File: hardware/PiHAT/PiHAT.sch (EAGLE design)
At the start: 1 part

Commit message: Bulk copy/paste schematic
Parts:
- added C1, C16, C17, C6, C9: 1uF, SparkFun-Capacitors:CAP0805
- added C10, C11: 0.1uF, SparkFun-Capacitors:CAP0805
- added C12, C13, C14, C15, C3, C4, C5, C7: 0.1uF, SparkFun-Passives:CAP0805
- added C2: 100pF, SparkFun-Capacitors:CAP0805
- added C8: 4.7uF, SparkFun-Capacitors:CAP0805
- added IAQ-CORE: IAQ-CORE, IAQ-CORE:IAQ-CORE
- added J2: (no value), SparkFun-Connectors:M05X2PTH
- added J3: USB-MICROB, SparkFun-Connectors:USB-MICROB
- added LED2, RX, TX: (no value), adafruit:LEDCHIPLED_0805
- added MICS4514: SPARKFUN-SENSORS_MICS-4514, MICS-4514_CO_and_NOx_Sensor_Breakout:SPARKFUN-SENSORS_MICS-4514
- added MOSFET: SPARKFUN-DISCRETESEMI_MOSFET-NCHANNELBSS138, MICS-4514_CO_and_NOx_Sensor_Breakout:SPARKFUN-DISCRETESEMI_MOSFET-NCHANNELBSS138
- added R1, R13, R7: 10K, SparkFun-Passives:RESISTOR0805-RES
- added R10, R9: 47, SparkFun-Passives:RESISTOR0805-RES
- added R11: SHOTTKY, SparkFun-Passives:RESISTOR0805-RES
- added R12, R21: 27, SparkFun-Passives:RESISTOR0805-RES
- added R14: 47K, SparkFun-Passives:RESISTOR0805-RES
- added R15, R18: 82, SparkFun-Passives:RESISTOR0805-RES
- added R16: 22K, SparkFun-Passives:RESISTOR0805-RES
- added R17: 51, SparkFun-Passives:RESISTOR0805-RES
- added R19, R8: 100K, SparkFun-Passives:RESISTOR0805-RES
- added R20: 100, SparkFun-Passives:RESISTOR0805-RES
- added R3: 1.5K, SparkFun-Passives:RESISTOR0805-RES
- added R4: 47, SparkFun-Resistors:RESISTOR0805-RES
- added R5, R6: 10K, SparkFun-Resistors:RESISTOR0805-RES
- added RESET: TAC_SWITCHSMD, SparkFun-Retired:TAC_SWITCHSMD
- added U$3: OPA344, SparkFun-AnalogIC:OPA344
- added U$4: RFM69HW, RFM69 USB Gateway:LOWPOWERLAB_RFM69
- added U1: ATMEGA328P, SparkFun-DigitalIC:ATMEGA328P_TQFP
- added U2: TSL2561, SparkFun-DigitalIC:TSL2561FN
- added U4: MPL115A, SparkFun-Sensors:MPL115A
- added U5: FT231XS, SparkFun-DigitalIC:FT231XS
- added U6: ADMP401, SparkFun-Sensors:ADMP401
- added U7: SHT31-DIS, thomasb9511:SHT31-DIS
- added U8, U9: MCP1703CB, linear:MCP1703CB
- added X1: (no value), adafruit:SMACONNECTOR_EDGE
- added Y1: 16MHZ, SparkFun-FreqCtrl:RESONATOR16MHZ
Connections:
- new net 5V: C17.1, C7.1, MICS4514.RH2_OX, MICS4514.RH2_RED, MICS4514.RS2_OX, MICS4514.RS2_RED, U9.VO
- new net A0: C2.2, R8.1, U$3.OUT, U1.PC0(ADC0)
- new net A7: U1.ADC7
- new net ANT: U$4.ANT, X1.ANT
- new net D2: U$4.DIO0, U1.PD2(INT0)
- new net D5: U1.PD5(T1)
- new net DTR: C12.1, J2.10, U5.!DTR
- new net FTDI_VCC: R10.1, R9.1, U5.!RESET, U5.3V3OUT, U5.VCCIO
- new net MISO: J2.1, U$4.MISO, U1.PB4(MISO)
- new net MOSI: J2.4, U$4.MOSI, U1.PB3(MOSI/OC2)
- new net N$10: C2.1, R3.1, R8.2, U$3.-IN
- new net N$11: C9.1, R1.2, R7.1, U$3.+IN
- new net N$12: C13.1, U4.CAP
- new net N$13: MICS4514.RH1_RED, R15.2
- new net N$17: RX.C, U5.CBUS1
- new net N$18: TX.C, U5.CBUS2
- new net N$2: R4.1, U1.PB1(OC1A)
- new net N$20: MOSFET.D, R17.2, R18.1
- new net N$23: MOSFET.G, R19.2, R20.1
- new net N$25: R21.1, U5.USBDM
- new net N$26: R12.1, U5.USBDP
- new net N$27: R9.2, RX.A
- new net N$29: R10.2, TX.A
- new net N$3: LED2.A, R4.2
- new net N$32: J3.D-, R21.2
- new net N$33: J3.D+, R12.2
- new net N$4: U1.PB7(XTAL2/TOSC2), Y1.3
- new net N$5: U1.PB6(XTAL1/TOSC1), Y1.1
- new net N$7: C8.1, U6.OUT
- new net N$8: MICS4514.RH1_OX, R18.2
- new net N$9: C8.2, R3.2
- new net PRE: R20.2, U1.PD3(INT1)
- new net PWR: C1.1, C16.1, J2.2, R11.1, U8.VI, U9.VI
- new net RESET: C12.2, J2.5, R13.1, RESET.3, RESET.4, U1.PC6(/RESET)
- new net RX: J2.7, U1.PD0(RXD), U5.TXD
- new net SCK: J2.3, U$4.SCK, U1.PB5(SCK)
- new net SS: J2.9, U$4.SEL, U1.PB2(SS/OC1B)
- new net TX: J2.8, U1.PD1(TXD), U5.RXD
- new net VBUS: C11.1, J3.VBUS, R11.2, U5.VCC
- new net VCC: C10.1, C14.1, C15.1, C3.1, C4.1, C5.1, C6.1, IAQ-CORE.VCC, R13.2, R5.2, R6.2, R7.2, U$3.V+, U$4.VCC, U1.AVCC, U1.VCC@4, U1.VCC@6, U2.VDD, U4.SHDN, U4.VDD, U6.VDD, U7.VCC, U8.VO
- new net VNOX: MICS4514.RS1_OX, R16.2, U1.PC1(ADC1)
- new net VRED: MICS4514.RS1_RED, R14.2, U1.PC2(ADC2)
- net GND: now also C1.2, C10.2, C11.2, C13.2, C14.2, C15.2, C16.2, C17.2, C3.2, C4.2, C5.2, C6.2, C7.2, C9.2, IAQ-CORE.GND, J2.6, J3.GND, LED2.C, MOSFET.S, R1.1, R14.1, R15.1, R16.1, R17.1, R19.1, RESET.1, RESET.2, U$3.V-, U$4.GND, U1.AGND, U1.GND@3, U1.GND@5, U2.GND, U4.GND, U5.GND@16, U5.GND@6, U6.GND@2, U6.GND@4, U6.GND@6, U7.ADDR, U7.GND, U7.NC, U8.GND, U9.GND, X1.GND1, X1.GND2, X1.GND3, X1.GND4, Y1.2
- net SCL: now also IAQ-CORE.SCL, R6.1, U1.PC5(ADC5/SCL), U2.SCL, U4.SCLK, U7.SCL
- net SDA: now also IAQ-CORE.SDA, R5.1, U1.PC4(ADC4/SDA), U2.SDA, U4.SDA/DIN, U7.SDA
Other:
- note added: "0x39"
- note added: "0x44"
- note added: "0x5A"
- note added: "0x60"
- note added: "3.3V voltage regulator"
- note added: "5V voltage regulator"
- note added: "Air Pressure"
- note added: "CO and NO2 concentration"
- note added: "CRT Labs"
- note added: "Designed by Akram Ali and Dave Conroy"
- note added: "ISP"
- note added: "Light Intensity"
- note added: "RFM69HW"
- note added: "Sensor Node"
- note added: "Sound Intensity"
- note added: "Temperature and Relative Humidity"
- note added: "USB + FTDI"
- note added: "VOC and Derived CO2"
- note added: "v0.5 (September 2016)"

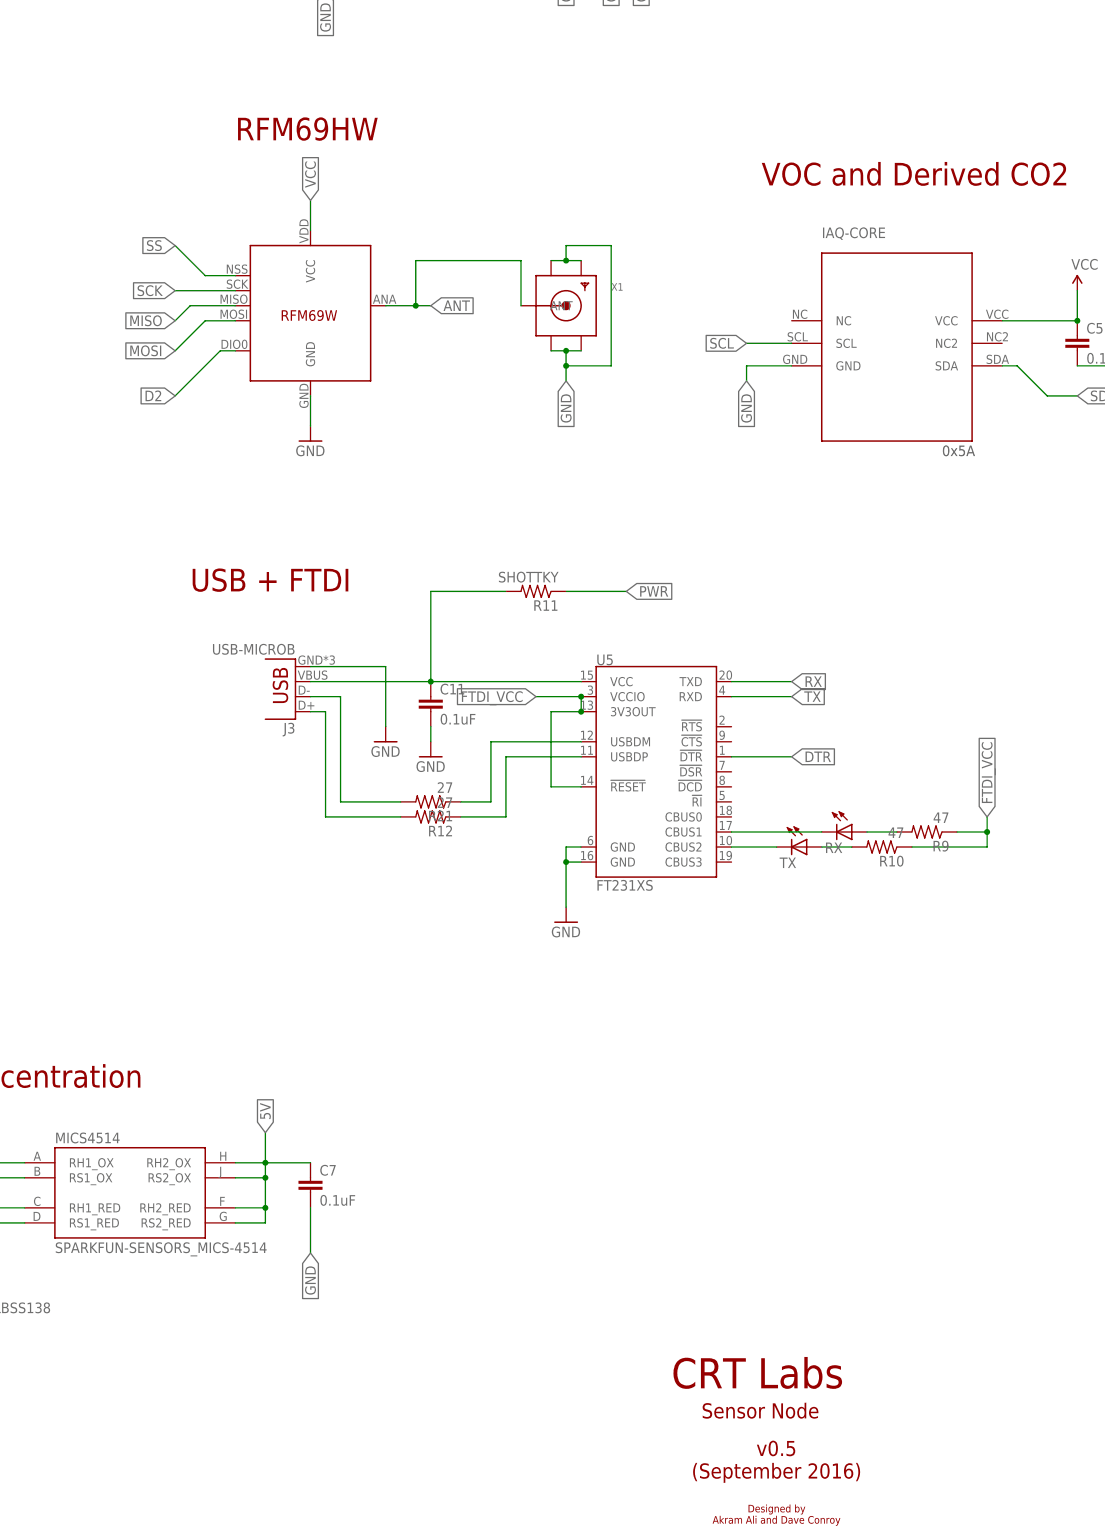
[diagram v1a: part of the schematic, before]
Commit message: Removed FTDI, RFM69, USB
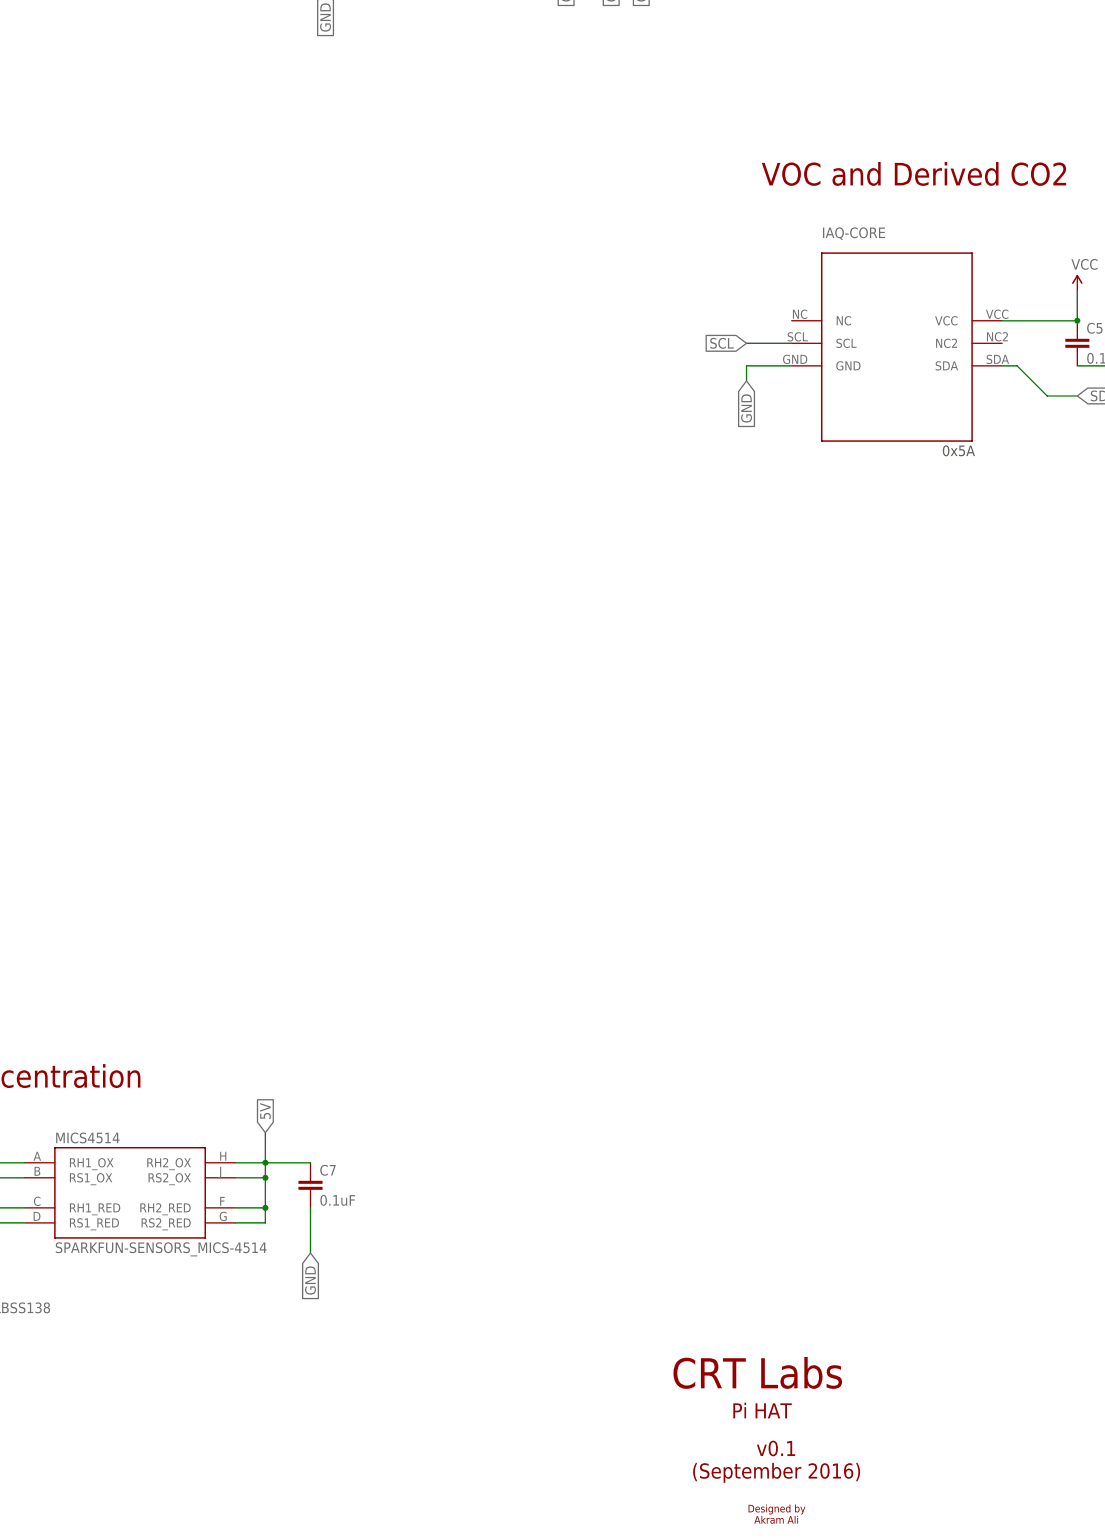
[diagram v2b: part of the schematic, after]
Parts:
- removed C11: 0.1uF, SparkFun-Capacitors:CAP0805
- removed J3: USB-MICROB, SparkFun-Connectors:USB-MICROB
- removed R10, R9: 47, SparkFun-Passives:RESISTOR0805-RES
- removed R11: SHOTTKY, SparkFun-Passives:RESISTOR0805-RES
- removed R12, R21: 27, SparkFun-Passives:RESISTOR0805-RES
- removed RX, TX: (no value), adafruit:LEDCHIPLED_0805
- removed U$4: RFM69HW, RFM69 USB Gateway:LOWPOWERLAB_RFM69
- removed U5: FT231XS, SparkFun-DigitalIC:FT231XS
- removed X1: (no value), adafruit:SMACONNECTOR_EDGE
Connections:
- removed net ANT: U$4.ANT, X1.ANT
- removed net FTDI_VCC: R10.1, R9.1, U5.!RESET, U5.3V3OUT, U5.VCCIO
- removed net N$17: RX.C, U5.CBUS1
- removed net N$18: TX.C, U5.CBUS2
- removed net N$25: R21.1, U5.USBDM
- removed net N$26: R12.1, U5.USBDP
- removed net N$27: R9.2, RX.A
- removed net N$29: R10.2, TX.A
- removed net N$32: J3.D-, R21.2
- removed net N$33: J3.D+, R12.2
- removed net VBUS: C11.1, J3.VBUS, R11.2, U5.VCC
- net D2: no longer U$4.DIO0
- net DTR: no longer U5.!DTR
- net GND: no longer C11.2, J3.GND, U$4.GND, U5.GND@16, U5.GND@6, X1.GND1, X1.GND2, X1.GND3, X1.GND4
- net MISO: no longer U$4.MISO
- net MOSI: no longer U$4.MOSI
- net PWR: no longer R11.1
- net RX: no longer U5.TXD
- net SCK: no longer U$4.SCK
- net SS: no longer U$4.SEL
- net TX: no longer U5.RXD
- net VCC: no longer U$4.VCC
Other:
- note added: "Designed by Akram Ali"
- note added: "Pi HAT"
- note added: "v0.1 (September 2016)"
- note removed: "Designed by Akram Ali and Dave Conroy"
- note removed: "RFM69HW"
- note removed: "Sensor Node"
- note removed: "USB + FTDI"
- note removed: "v0.5 (September 2016)"

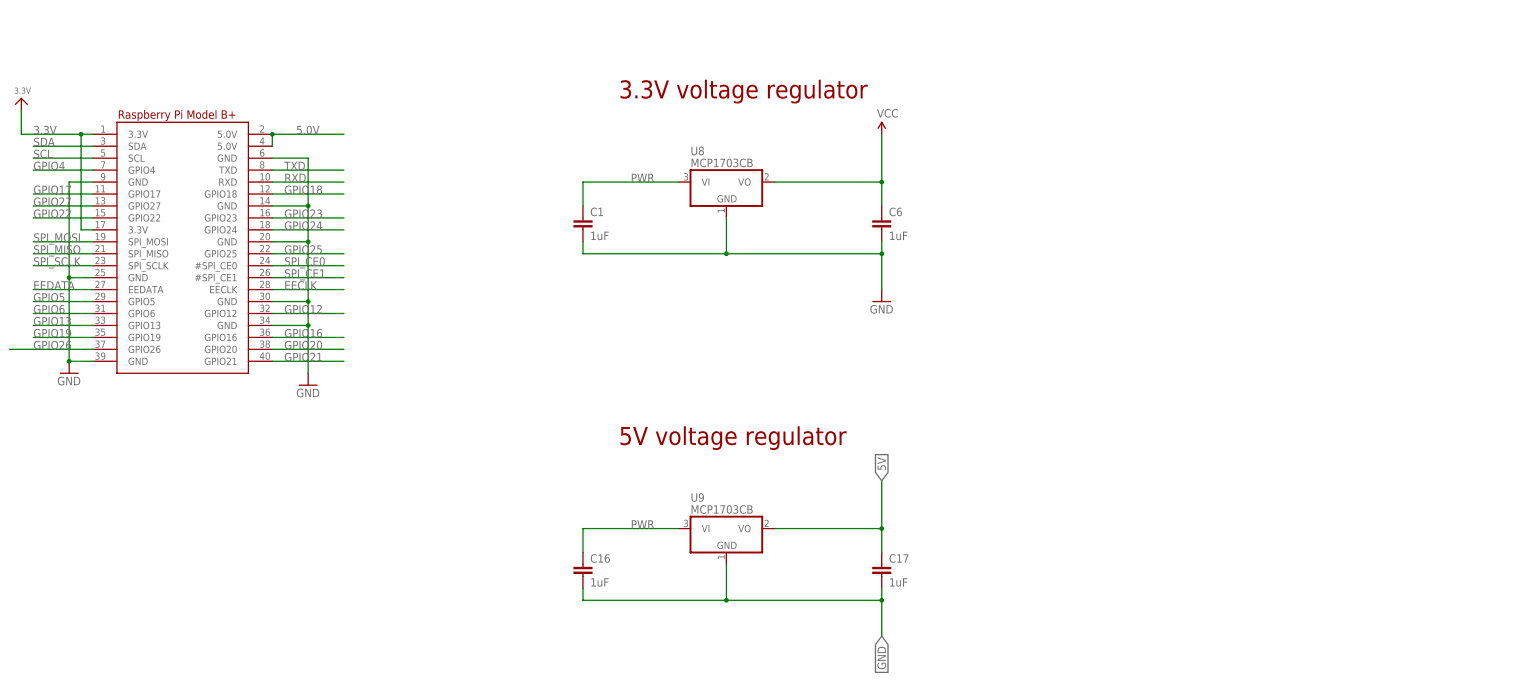
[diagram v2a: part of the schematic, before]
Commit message: started mapping sensors for pi hat
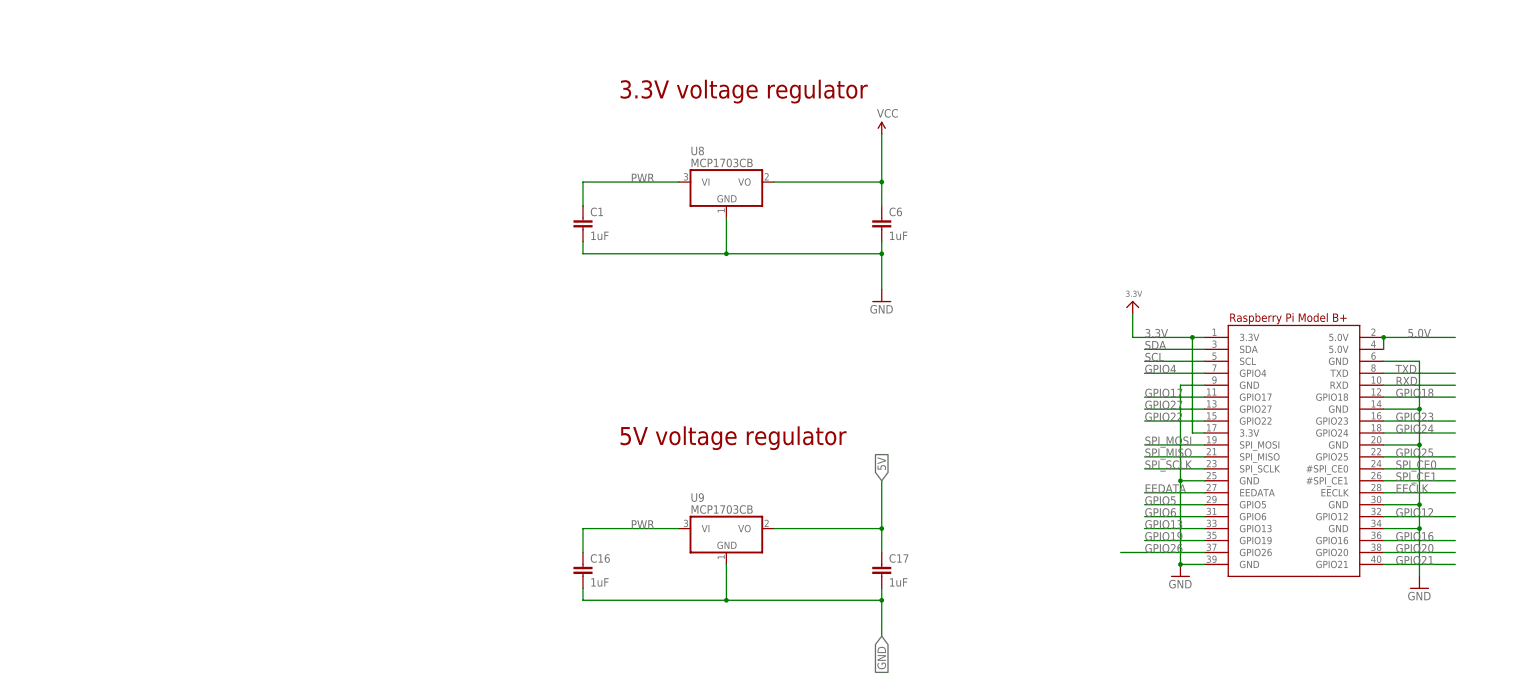
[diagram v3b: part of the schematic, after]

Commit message: All traces routed - v0.1
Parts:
- removed C1, C16, C17, C6: 1uF, SparkFun-Capacitors:CAP0805
- removed U8, U9: MCP1703CB, linear:MCP1703CB
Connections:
- removed net 3.3V: RPI1.3.3V, RPI1.3.3V@1
- removed net 5.0V: RPI1.5.0V, RPI1.5.0V@1
- net 5V: now also RPI1.5.0V, RPI1.5.0V@1; no longer C17.1, U9.VO
- net GND: no longer C1.2, C16.2, C17.2, C6.2, U8.GND, U9.GND
- net PWR: no longer C1.1, C16.1, U8.VI, U9.VI
- net VCC: now also RPI1.3.3V, RPI1.3.3V@1; no longer C6.1, U8.VO
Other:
- note removed: "3.3V voltage regulator"
- note removed: "5V voltage regulator"

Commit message: Fixed several traces
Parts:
- renumbered U$3 to U3
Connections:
- new net PI_SCL: RPI1.SCL
- new net PI_SDA: RPI1.SDA
- net SCL: no longer RPI1.SCL
- net SDA: no longer RPI1.SDA
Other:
- moved on the sheet: C13, C14, C3, C5, C7, IAQ-CORE, J2, MICS4514, MOSFET, R14, R15, R16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
